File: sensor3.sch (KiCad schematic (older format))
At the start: 19 parts, among them CON1 AVR-ISP-6, CON2 DM3AT-SF-PEJM5, IC1 ATMEGA328P-A, P1 POWER, P2 RX/TX, P3 I2C, SW1 START/STOP, SW2 FORMAT, U1 AE-LPS331AP, U2 SL-MPU9150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

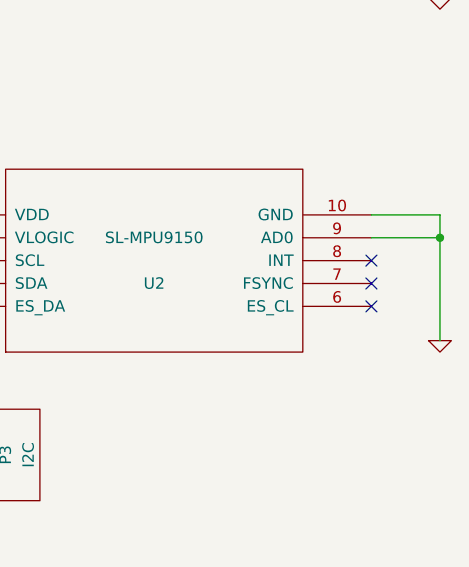
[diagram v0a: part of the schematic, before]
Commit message: Connect FSYNC to GND
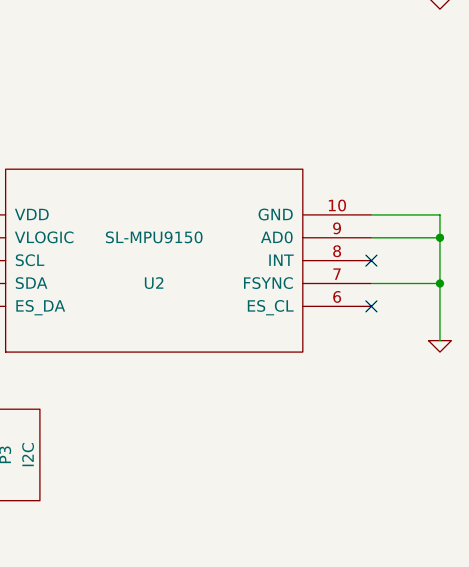
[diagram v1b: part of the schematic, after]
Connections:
- net GND: now also U2.7 (FSYNC)
- no-connect marks 24 -> 23
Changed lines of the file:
@@
 Sheet 1 1
 Title "sensor3"
-Date "18 jan 2015"
+Date "28 jan 2015"
 Rev "A"
 Comp ""
@@
 Connection ~ 11000 3800
 NoConn ~ 10700 3900
-NoConn ~ 10700 4000
 NoConn ~ 10700 4100
 NoConn ~ 10700 2250
@@
 Wire Wire Line
 	8600 4600 8800 4600
+Wire Wire Line
+	10700 4000 11000 4000
+Connection ~ 11000 4000
 $EndSCHEMATC
